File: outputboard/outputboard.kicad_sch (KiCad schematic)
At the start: 11 parts, among them J1 Conn_01x05_Male, J2 AudioJack4, Q1 2N2222A, SW1 SW_SPDT

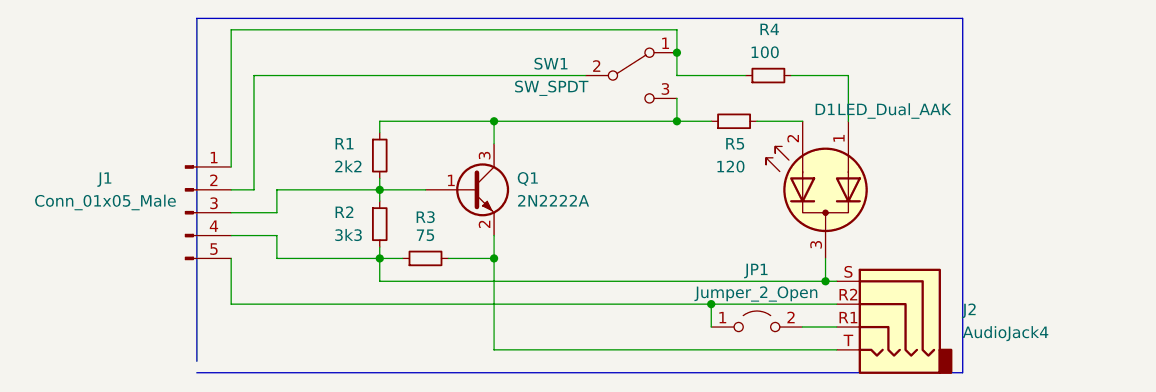
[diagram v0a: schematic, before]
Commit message: add part description for more complex parts, remove unused cap
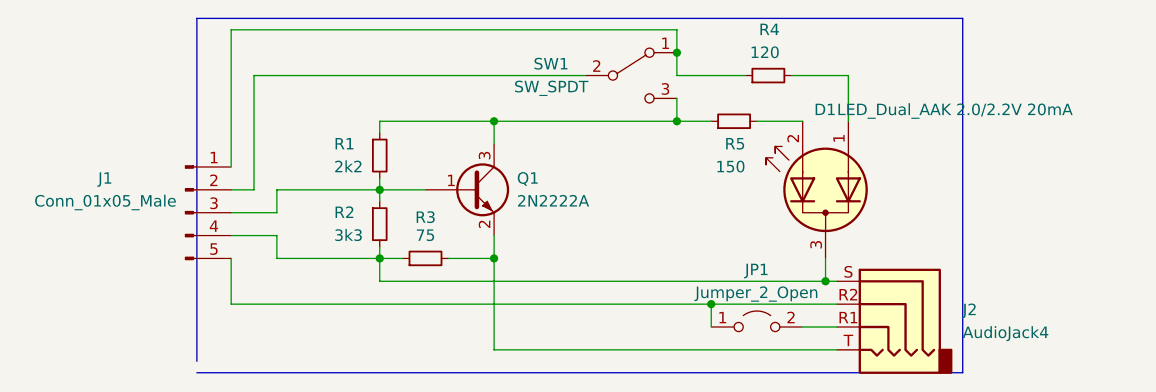
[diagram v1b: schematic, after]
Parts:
- D1: value LED_Dual_AAK -> LED_Dual_AAK 2.0/2.2V 20mA; Part (none) -> Kingbright KM23ESGW
- J1: Part (none) -> Amtek 2542R-05TW-L; Part (Alt 1) (none) -> JST like JH2.54-5 (Part of X0014J7UB1)
- J2: Part (none) -> Tensility 54-00177
- Q1: Part (none) -> Nexperia PMBT2222A
- R4: value 100 -> 120
- R5: value 120 -> 150
- SW1: Part (none) -> Würth WS-SLSU 450404015514
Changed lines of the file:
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@@
+      (effects (font (size 1.27 1.27)) hide)
+    )
+    (property "Part" "Tensility 54-00177" (id 4) (at 193.04 105.41 0)
       (effects (font (size 1.27 1.27)) hide)
     )
@@
       (effects (font (size 1.27 1.27)) (justify right))
     )
-    (property "Value" "LED_Dual_AAK" (id 1) (at 187.96 83.82 90)
+    (property "Value" "LED_Dual_AAK 2.0/2.2V 20mA" (id 1) (at 187.96 83.82 90)
       (effects (font (size 1.27 1.27)) (justify right))
     )
@@
       (effects (font (size 1.27 1.27)) hide)
     )
+    (property "Part" "Kingbright KM23ESGW" (id 4) (at 186.69 92.71 90)
+      (effects (font (size 1.27 1.27)) hide)
+    )
     (pin "1")
     (pin "2")
@@
       (effects (font (size 1.27 1.27)) (justify left))
     )
-    (property "Value" "100" (id 1) (at 181.61 77.47 90)
+    (property "Value" "120" (id 1) (at 181.61 77.47 90)
       (effects (font (size 1.27 1.27)) (justify left))
     )
@@
       (effects (font (size 1.27 1.27)) hide)
     )
+    (property "Part" "Amtek 2542R-05TW-L" (id 4) (at 115.57 95.25 0)
+      (effects (font (size 1.27 1.27)) hide)
+    )
+    (property "Part (Alt 1)" "JST like JH2.54-5 (Part of X0014J7UB1)" (id 5) (at 115.57 95.25 0)
+      (effects (font (size 1.27 1.27)) hide)
+    )
     (pin "1")
     (pin "2")
@@
       (effects (font (size 1.27 1.27)) hide)
     )
+    (property "Part" "Würth WS-SLSU 450404015514" (id 4) (at 165.1 80.01 0)
+      (effects (font (size 1.27 1.27)) hide)
+    )
     (pin "1")
     (pin "2")
@@
       (effects (font (size 1.27 1.27)) (justify left))
     )
-    (property "Value" "120" (id 1) (at 177.8 90.17 90)
+    (property "Value" "150" (id 1) (at 177.8 90.17 90)
       (effects (font (size 1.27 1.27)) (justify left))
     )
@@
     )
     (property "Datasheet" "~" (id 3) (at 147.32 92.71 0)
+      (effects (font (size 1.27 1.27)) hide)
+    )
+    (property "Part" "Nexperia PMBT2222A" (id 4) (at 147.32 92.71 0)
       (effects (font (size 1.27 1.27)) hide)
     )
@@
   (symbol_instances
     (path "/4d18e310-c3a3-43c0-b623-266032271258"
-      (reference "D1") (unit 1) (value "LED_Dual_AAK") (footprint "Package_TO_SOT_SMD:SOT-23_Handsoldering")
+      (reference "D1") (unit 1) (value "LED_Dual_AAK 2.0/2.2V 20mA") (footprint "Package_TO_SOT_SMD:SOT-23_Handsoldering")
     )
     (path "/6c6c7128-3cd5-4146-bd49-7a6fa7da139e"
@@
     )
     (path "/519f4229-95b3-4e1f-85e9-243c592c7211"
-      (reference "R4") (unit 1) (value "100") (footprint "Resistor_SMD:R_1206_3216Metric_Pad1.30x1.75mm_HandSolder")
+      (reference "R4") (unit 1) (value "120") (footprint "Resistor_SMD:R_1206_3216Metric_Pad1.30x1.75mm_HandSolder")
     )
     (path "/c154a15b-2c7f-4b1f-8af8-df966ec54964"
-      (reference "R5") (unit 1) (value "120") (footprint "Resistor_SMD:R_1206_3216Metric_Pad1.30x1.75mm_HandSolder")
+      (reference "R5") (unit 1) (value "150") (footprint "Resistor_SMD:R_1206_3216Metric_Pad1.30x1.75mm_HandSolder")
     )
     (path "/b5556445-1554-4bc1-8f96-85e48794e2d8"

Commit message: add some more parts, use 0805 components for C53 & C54
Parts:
- R1: Part (none) -> Yageo RC1206JR-072K2L
- R2: Part (none) -> Yageo RC1206JR-073K3L
- R3: Part (none) -> Yageo RC1206JR-0775RL
- R4: Part (none) -> Yageo RC1206FR-07120RL
- R5: Part (none) -> Yageo RC1206FR-13150RL
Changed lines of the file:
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@@
+      (effects (font (size 1.27 1.27)) hide)
+    )
+    (property "Part" "Yageo RC1206JR-072K2L" (id 4) (at 137.16 88.9 0)
       (effects (font (size 1.27 1.27)) hide)
     )
@@
     )
     (property "Datasheet" "~" (id 3) (at 180.34 80.01 0)
+      (effects (font (size 1.27 1.27)) hide)
+    )
+    (property "Part" "Yageo RC1206FR-07120RL" (id 4) (at 180.34 80.01 90)
       (effects (font (size 1.27 1.27)) hide)
     )
@@
       (effects (font (size 1.27 1.27)) hide)
     )
+    (property "Part" "Yageo RC1206JR-073K3L" (id 4) (at 137.16 96.52 0)
+      (effects (font (size 1.27 1.27)) hide)
+    )
     (pin "1")
     (pin "2")
@@
     )
     (property "Datasheet" "~" (id 3) (at 176.53 85.09 0)
+      (effects (font (size 1.27 1.27)) hide)
+    )
+    (property "Part" "Yageo RC1206FR-13150RL" (id 4) (at 176.53 85.09 90)
       (effects (font (size 1.27 1.27)) hide)
     )
@@
       (effects (font (size 1.27 1.27)) hide)
     )
+    (property "Part" "Yageo RC1206JR-0775RL" (id 4) (at 142.24 100.33 90)
+      (effects (font (size 1.27 1.27)) hide)
+    )

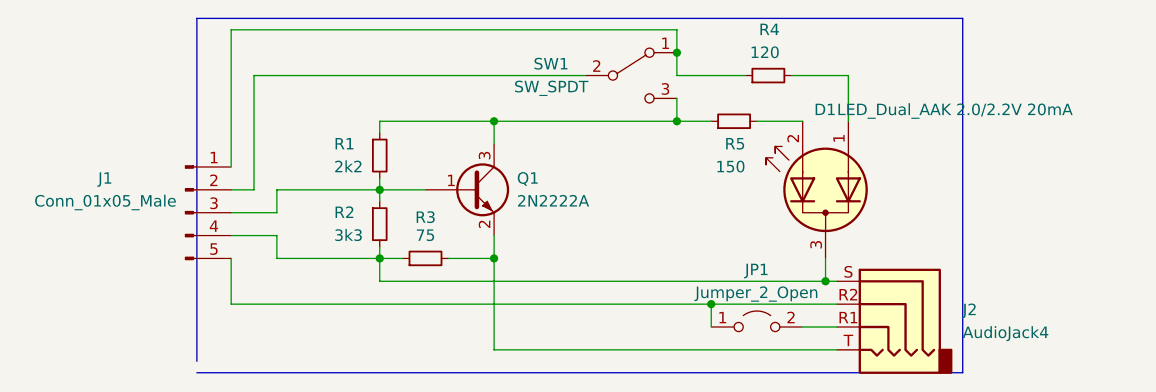
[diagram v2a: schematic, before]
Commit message: update to Kicad 8
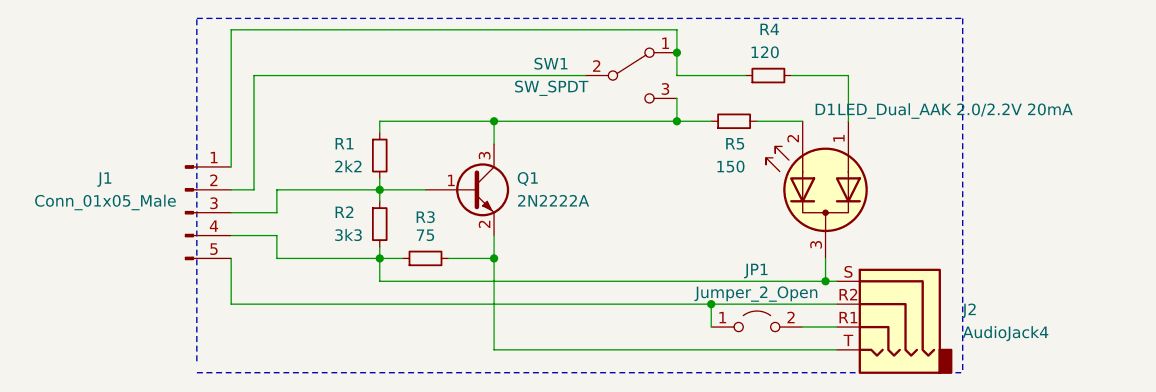
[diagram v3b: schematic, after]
